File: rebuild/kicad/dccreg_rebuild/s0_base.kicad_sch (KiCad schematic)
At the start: 8 parts

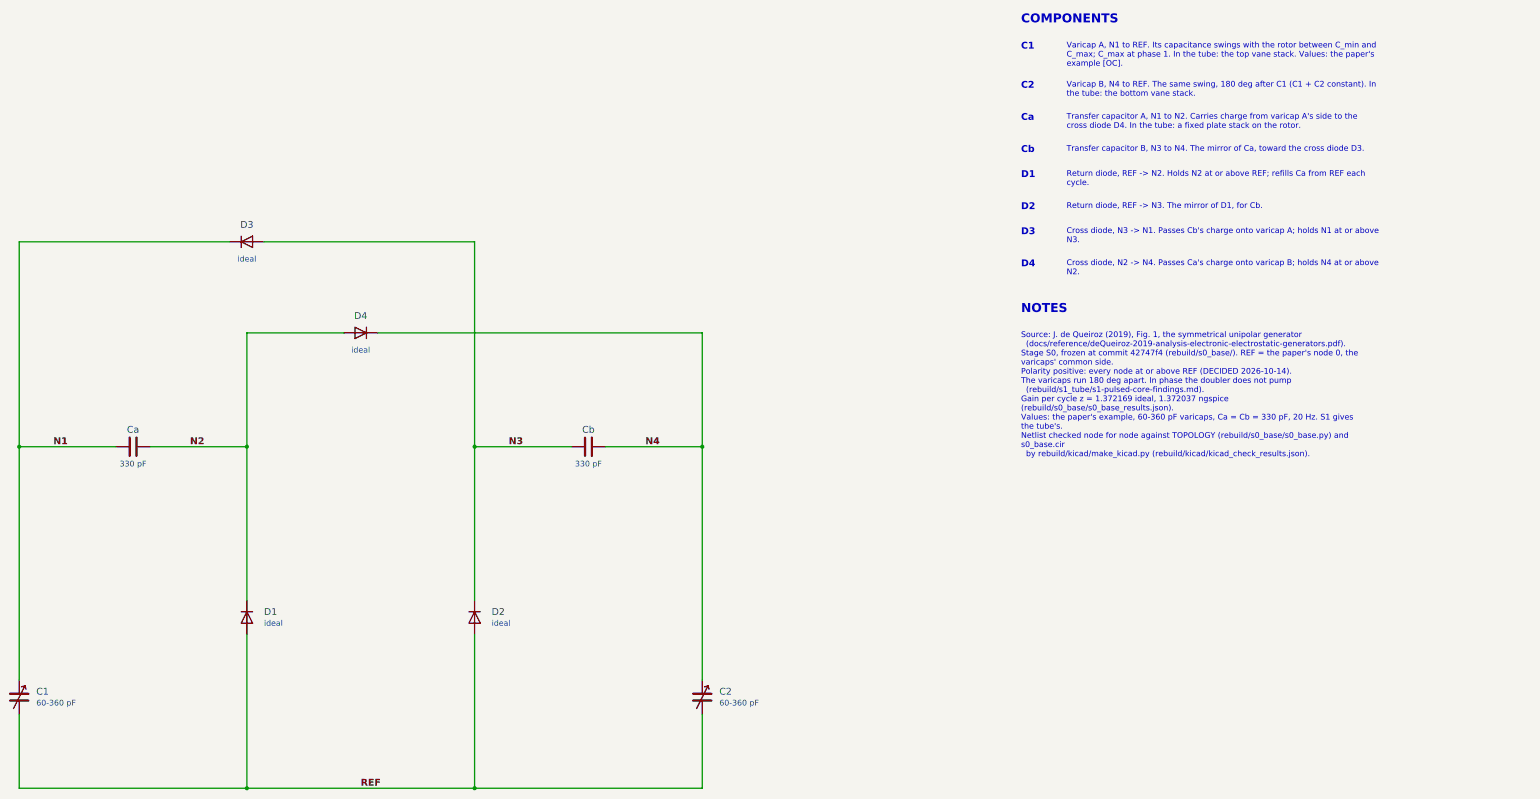
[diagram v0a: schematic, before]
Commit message: feat(rebuild): one KiCad project with a sheet per stage
The designer asked for all stages and changes in one project, each on
its own sheet. rebuild/kicad/dccreg_rebuild/ replaces the two separate
projects: a root sheet indexes the stages, with S0 and S1 as sheets 2
and 3. Each stage numbers its parts in its own hundred (S0 1xx, S1 2xx),
and the nets stay local to their sheet. The layout the designer accepted
is unchanged.

The check exports the project netlist, cuts it by sheet and compares each
stage with its source: S0 against TOPOLOGY and s0_base.cir, S1 against
TOPOLOGY plus the additions and the pulsed-core solver. All match, and
the ERC is clean. A new stage is one entry in STAGES.

Co-Authored-By: Claude Opus 5.5 <noreply@anthropic.com>
Claude-Session: https://claude.ai/code/session_01EZwGpTFL1hyaEya41kJtBw
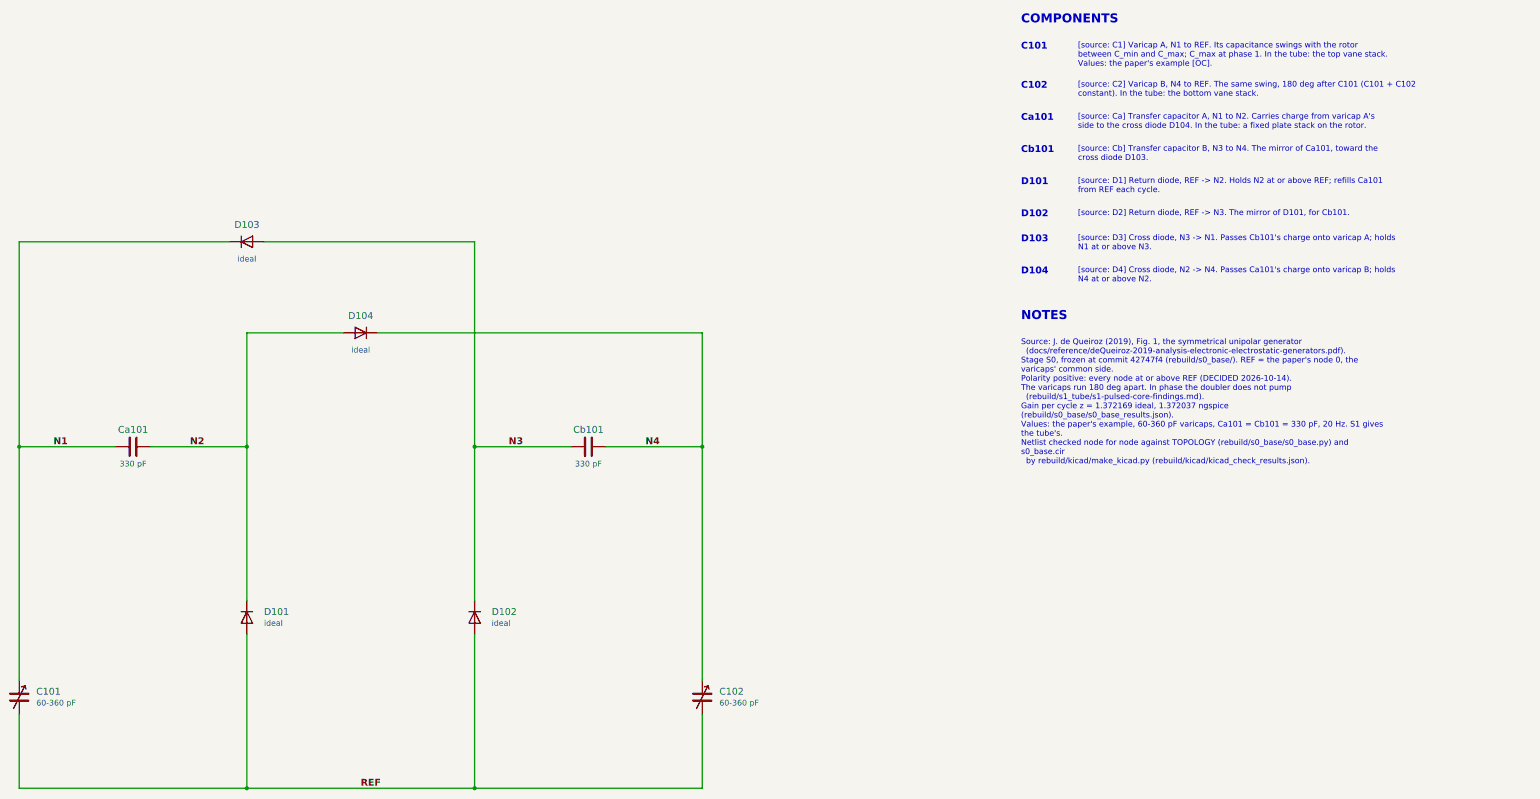
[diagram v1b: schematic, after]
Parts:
- renumbered C1 to C101, C2 to C102, Ca to Ca101, Cb to Cb101, D1 to D101, D2 to D102, D3 to D103, D4 to D104
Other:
- note added: "C101"
- note added: "C102"
- note added: "Ca101"
- note added: "Cb101"
- note added: "D101"
- note added: "D102"
- note added: "D103"
- note added: "D104"
- note added: "[source: C1] Varicap A, N1 to REF. Its capacitance swings with the rotor between C_min and C_max; C_max at phase 1. In the tube: the top vane stack. Values: the paper's example [OC]."
- note added: "[source: C2] Varicap B, N4 to REF. The same swing, 180 deg after C101 (C101 + C102 constant). In the tube: the bottom vane stack."
- note added: "[source: Ca] Transfer capacitor A, N1 to N2. Carries charge from varicap A's side to the cross diode D104. In the tube: a fixed plate stack on the rotor."
- note added: "[source: Cb] Transfer capacitor B, N3 to N4. The mirror of Ca101, toward the cross diode D103."
- note added: "[source: D1] Return diode, REF -> N2. Holds N2 at or above REF; refills Ca101 from REF each cycle."
- note added: "[source: D2] Return diode, REF -> N3. The mirror of D101, for Cb101."
- note added: "[source: D3] Cross diode, N3 -> N1. Passes Cb101's charge onto varicap A; holds N1 at or above N3."
- note added: "[source: D4] Cross diode, N2 -> N4. Passes Ca101's charge onto varicap B; holds N4 at or above N2."
- note removed: "C1"
- note removed: "C2"
- note removed: "Ca"
- note removed: "Cb"
- note removed: "Cross diode, N2 -> N4. Passes Ca's charge onto varicap B; holds N4 at or above N2."
- note removed: "Cross diode, N3 -> N1. Passes Cb's charge onto varicap A; holds N1 at or above N3."
- note removed: "D1"
- note removed: "D2"
- note removed: "D3"
- note removed: "D4"
- note removed: "Return diode, REF -> N2. Holds N2 at or above REF; refills Ca from REF each cycle."
- note removed: "Return diode, REF -> N3. The mirror of D1, for Cb."
- note removed: "Transfer capacitor A, N1 to N2. Carries charge from varicap A's side to the cross diode D4. In the tube: a fixed plate stack on the rotor."
- note removed: "Transfer capacitor B, N3 to N4. The mirror of Ca, toward the cross diode D3."
- note removed: "Varicap A, N1 to REF. Its capacitance swings with the rotor between C_min and C_max; C_max at phase 1. In the tube: the top vane stack. Values: the paper's example [OC]."
- note removed: "Varicap B, N4 to REF. The same swing, 180 deg after C1 (C1 + C2 constant). In the tube: the bottom vane stack."

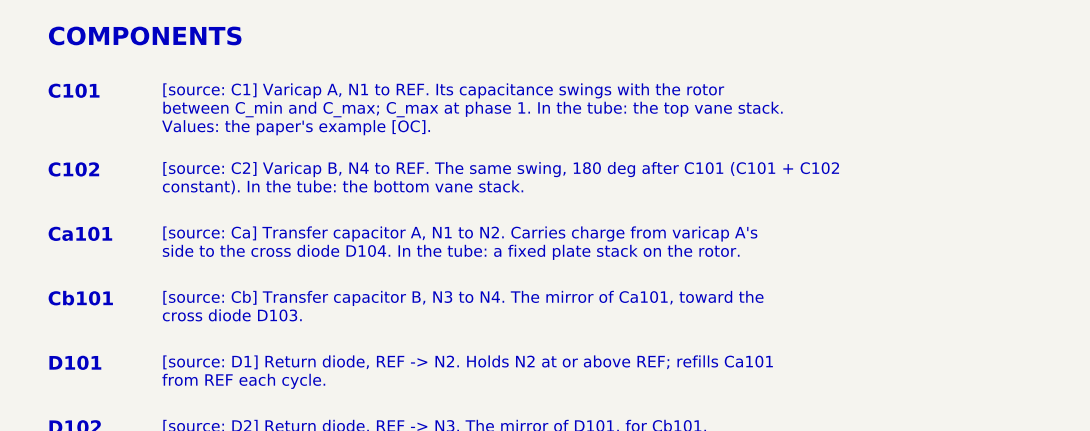
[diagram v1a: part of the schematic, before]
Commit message: feat(rebuild): S2 begins, the plan and the compact deck
The designer's starting choices for S2 (the 3-D models): the 10-11
redesign layout stripped back to the S1b circuit, N1 on side A below the
hub as the record, a rim variant to win back kappa, and the repo's
finite-volume field solver. FreeCAD 1.1.4 is installed beside KiCad.
rebuild/s2_models/s2-plan.md sets out S2a-S2d.

rebuild/s2_models/s2_deck.py plans the deck for the S1b parts only (the
designer: "a bigger deck then required would insert an unnecessary
compromise"), on the redesign study's rules:
- every HV part also clears the grounded can in air (the designer's
  choice): deck r 50-125 against the redesign's r 50-150;
- each clamp string split into two series halves placed against the
  sticks, so the deck balances to 9 g, where a chain plan needed 388 g;
- the column 13 mm off the deck instead of 39, so each side is 26 mm
  shorter;
- the cross wires run straight across, held at the midplane by a PTFE
  bracket with two ribs (41.9 mm creepage against 31.6 needed), as the
  designer asked for now.

Also corrected: N1 is side A (below the hub) in the S1 texts, the S1b
study (re-run, results unchanged) and the KiCad legends (regenerated;
netlists still match, ERC 0/0).

Co-Authored-By: Claude Opus 5.5 <noreply@anthropic.com>
Claude-Session: https://claude.ai/code/session_01EZwGpTFL1hyaEya41kJtBw
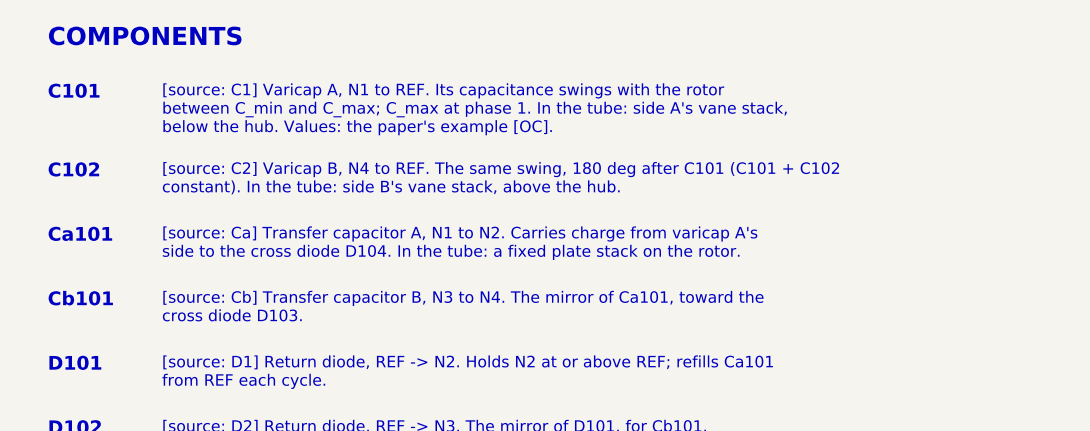
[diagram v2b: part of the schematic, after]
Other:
- note added: "[source: C1] Varicap A, N1 to REF. Its capacitance swings with the rotor between C_min and C_max; C_max at phase 1. In the tube: side A's vane stack, below the hub. Values: the paper's example [OC]."
- note added: "[source: C2] Varicap B, N4 to REF. The same swing, 180 deg after C101 (C101 + C102 constant). In the tube: side B's vane stack, above the hub."
- note removed: "[source: C1] Varicap A, N1 to REF. Its capacitance swings with the rotor between C_min and C_max; C_max at phase 1. In the tube: the top vane stack. Values: the paper's example [OC]."
- note removed: "[source: C2] Varicap B, N4 to REF. The same swing, 180 deg after C101 (C101 + C102 constant). In the tube: the bottom vane stack."
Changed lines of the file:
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@@
 		)
 	)
-	(text "[source: C1] Varicap A, N1 to REF. Its capacitance swings with the rotor\nbetween C_min and C_max; C_max at phase 1. In the tube: the top vane stack.\nValues: the paper's example [OC]."
+	(text "[source: C1] Varicap A, N1 to REF. Its capacitance swings with the rotor\nbetween C_min and C_max; C_max at phase 1. In the tube: side A's vane stack,\nbelow the hub. Values: the paper's example [OC]."
 		(exclude_from_sim yes)
 		(at 307.34 21.59 0)
@@
 		)
 	)
-	(text "[source: C2] Varicap B, N4 to REF. The same swing, 180 deg after C101 (C101 + C102\nconstant). In the tube: the bottom vane stack."
+	(text "[source: C2] Varicap B, N4 to REF. The same swing, 180 deg after C101 (C101 + C102\nconstant). In the tube: side B's vane stack, above the hub."
 		(exclude_from_sim yes)
 		(at 307.34 30.33 0)
@@
 			)
 		)
-		(property "Description" "Varicap A, N1 to REF. Its capacitance swings with the rotor between C_min and C_max; C_max at phase 1. In the tube: the top vane stack. Values: the paper's example [OC]."
+		(property "Description" "Varicap A, N1 to REF. Its capacitance swings with the rotor between C_min and C_max; C_max at phase 1. In the tube: side A's vane stack, below the hub. Values: the paper's example [OC]."
 			(at 71.12 167.64 0)
 			(hide yes)
@@
 			)
 		)
-		(property "Description" "Varicap B, N4 to REF. The same swing, 180 deg after C101 (C101 + C102 constant). In the tube: the bottom vane stack."
+		(property "Description" "Varicap B, N4 to REF. The same swing, 180 deg after C101 (C101 + C102 constant). In the tube: side B's vane stack, above the hub."
 			(at 223.52 167.64 0)
 			(hide yes)
